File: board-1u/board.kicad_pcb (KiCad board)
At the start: 2 copper layers, 70.1 x 22.5 mm, 39 parts, among them J1 Power, J10 B3, J11 B4, J2 A, J3 A1, J4 A2, J5 A3, J6 A4, J7 B, J8 B1, J9 B2, U1 OPA4991, U2 OPA4991, U3 LM358

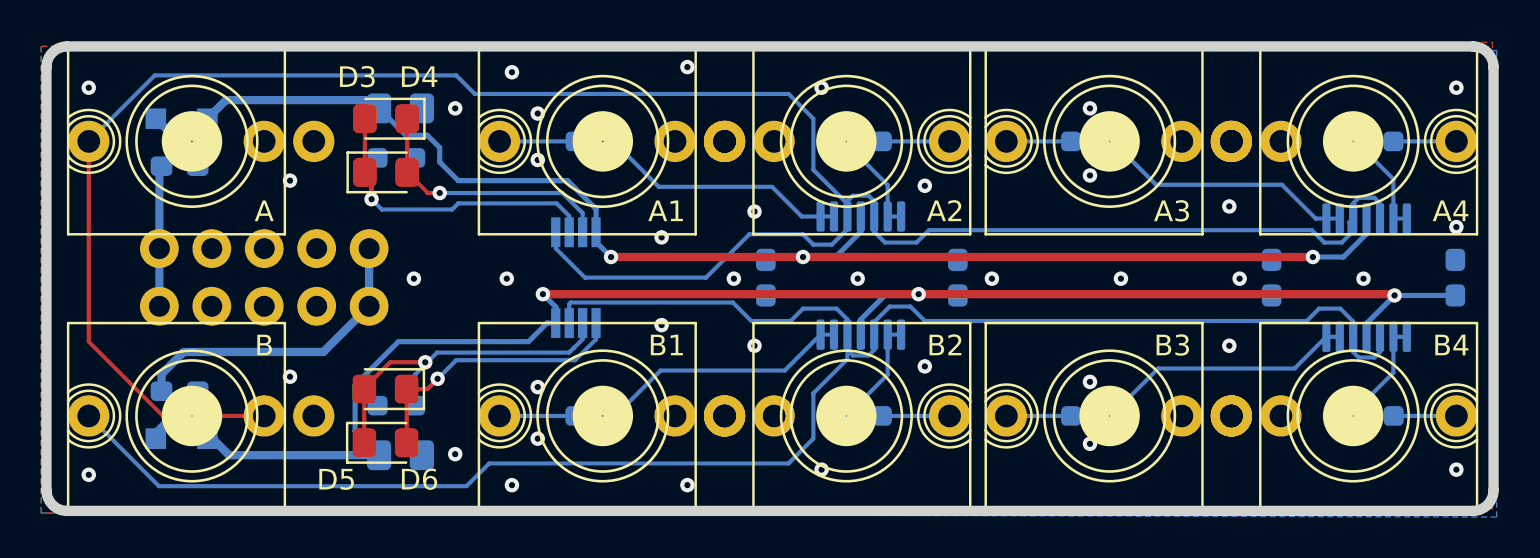
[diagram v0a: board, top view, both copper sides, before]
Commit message: Changes from tests on first revision
1. Silkscreen legibility changes
2. Added version numbers and such to page info blocks
3. Change MPNs and values
4. Change footprints for LEDs and Diodes.
5. Pin one markers
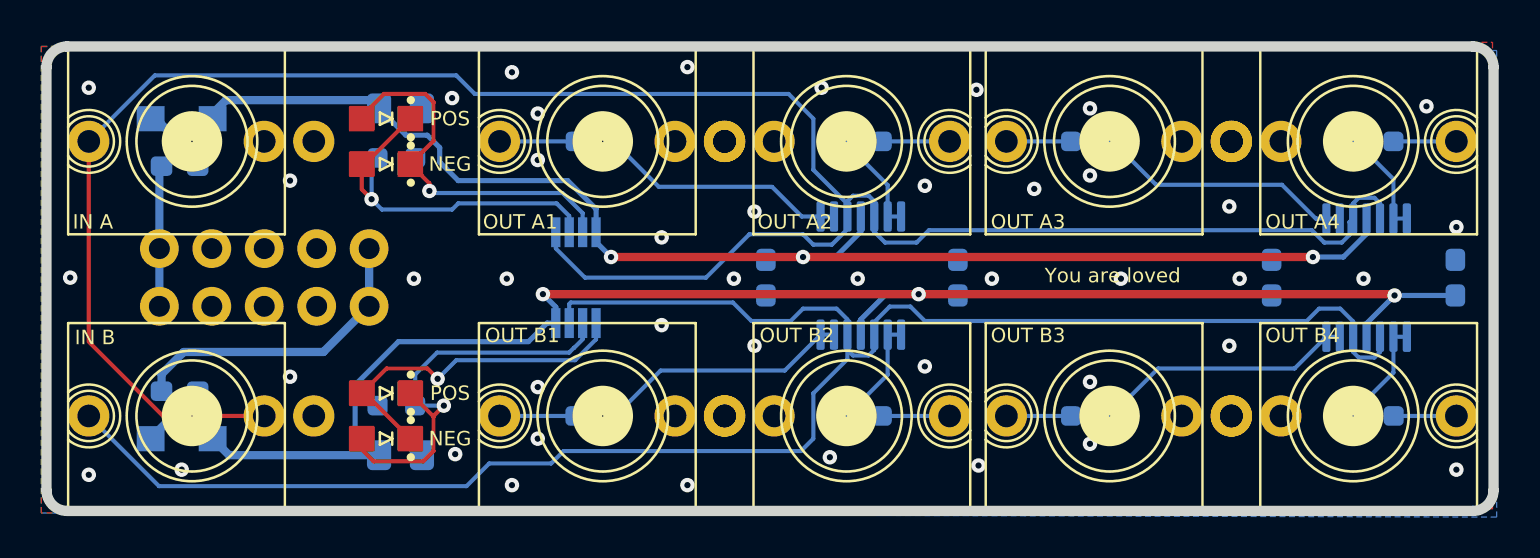
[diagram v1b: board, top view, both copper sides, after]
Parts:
- added REF**: OSHW-Logo2_7.3x6mm_SilkScreen, Symbol:OSHW-Logo2_7.3x6mm_SilkScreen, B.Cu at (152.1, 113.2)
- D1, D2: value 1N5819 -> BARRIER; footprint Diode_SMD:D_SOD-323_HandSoldering -> winterbloom:DIODE_SOD-123_SOD-123F
- D3, D4, D5, D6: footprint LED_SMD:LED_0805_2012Metric_Pad1.15x1.40mm_HandSolder -> winterbloom:LED_0805_Kingbright_APT2012
- FB1, FB2: value 300mA -> BEAD
- J10: value B3 -> OUT B3
- J11: value B4 -> OUT B4
- J2: value A -> IN A
- J3: value A1 -> OUT A1
- J4: value A2 -> OUT A2
- J5: value A3 -> OUT A3
- J6: value A4 -> OUT A4
- J7: value B -> IN B
- J8: value B1 -> OUT B1
- J9: value B2 -> OUT B2
- R10, R9: value 270 -> 270R
- moved D3 2.60 mm to (116.9, 103.7), turned to 180 degrees
- moved D5 2.40 mm to (116.9, 117.0), turned to 180 degrees
- moved D6 2.40 mm to (116.9, 119.2)
- moved D4 2.20 mm to (116.9, 105.9)
- moved G*** 1.00 mm to (157.6, 119.8)
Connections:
- J2 pad TN: Net-(J2-PadTN) -> GND
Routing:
- net Net-(D3-Pad2): track 12.8 -> 18.4 mm
- net Net-(D5-Pad1): track 17.2 -> 20.9 mm
- net Net-(D5-Pad2): track 13.6 -> 16.9 mm
- net Net-(D3-Pad1): track 17.1 -> 18.2 mm
- net GND: vias 39 -> 44
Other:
- board text added: "CERN-OHL-P V2 hydrogen.wntr.dev"
- board text added: "Hydrogen v2 10/2/2021"
- board text added: "PCB Specifications: - Dimensions: 22.5mm x 70.1mm - Thickness: 1.6mm - Layers: 2 - Min. track width: 0.2mm / 7 mil - Min. track spacing: 0.2mm / 7 mil - Min. drill: 0.4mm - Mask: Pink - Silk: Black or white - Surface finish: ENIG - Copper weight: 1oz - Substrate: FR4 Tg 140 or better - UL Marking: Bottom silk"
- board text added: "You are loved"
- board text removed: "Helium v1 9/19/21 CERN-OHL-P V2 helium.wntr.dev"
